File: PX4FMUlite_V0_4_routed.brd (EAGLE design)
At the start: 48.6 x 34.9 mm, 126 parts, among them J2 DF13-4P-1.25V, J201 DF13C-6P-1.25V, J202 DF13C-6P-1.25V, J203 DF13C-6P-1.25V, J3 DF13C-4P-1.25V, J302 DF13C-4P-1.25V, J401 DF13C-4P-1.25V, J403 DF13C-7P-1.25V, J405 DF13C-4P-1.25V, J802 DF13C-3P-1.25V, M3_MOUNT1101 MOUNT-HOLE3.1MM, M3_MOUNT1102 MOUNT-HOLE3.1MM, M3_MOUNT1103 MOUNT-HOLE3.1MM, M3_MOUNT1104 MOUNT-HOLE3.1MM, U101 STM32F4X7VX, U2 MAX3051, U401 MAX3051, X101 3.2x2.5 mm / 24 MHz / 15 ppm

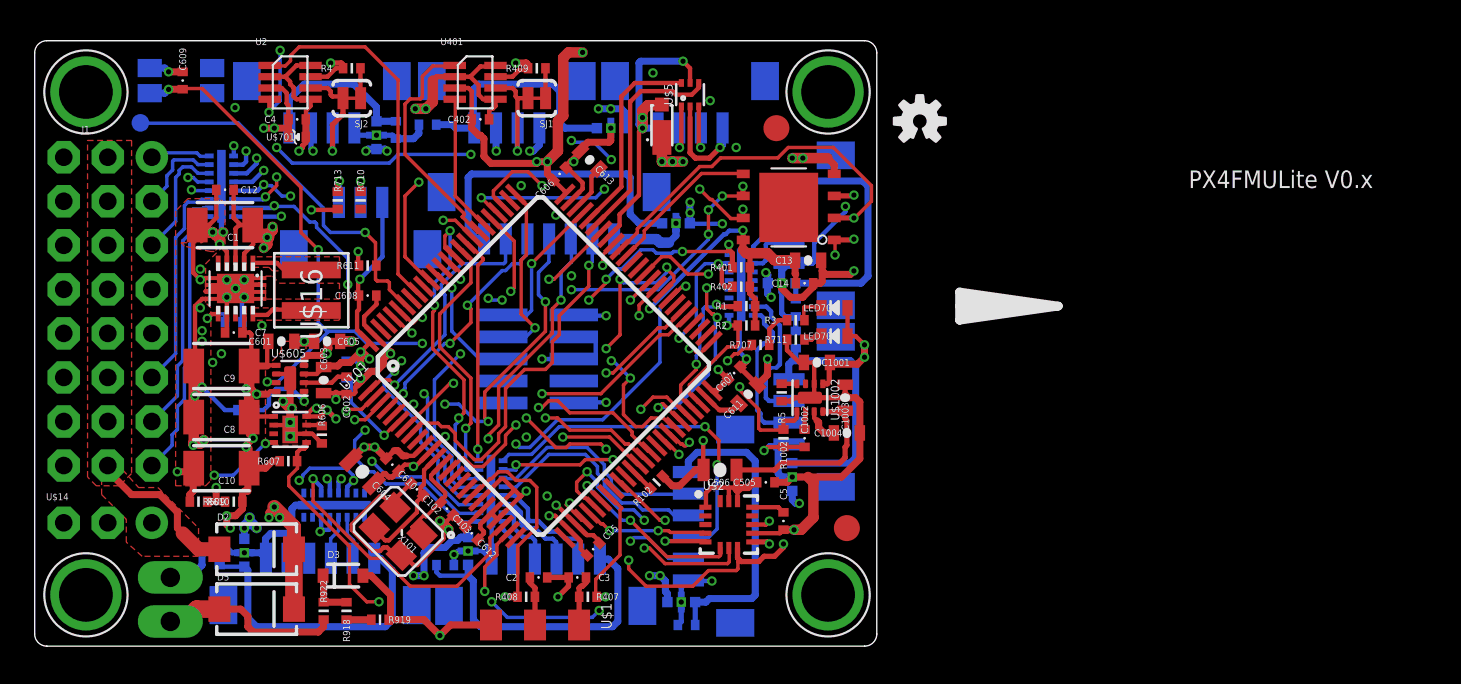
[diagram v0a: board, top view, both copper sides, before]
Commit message: Moved connector labeling
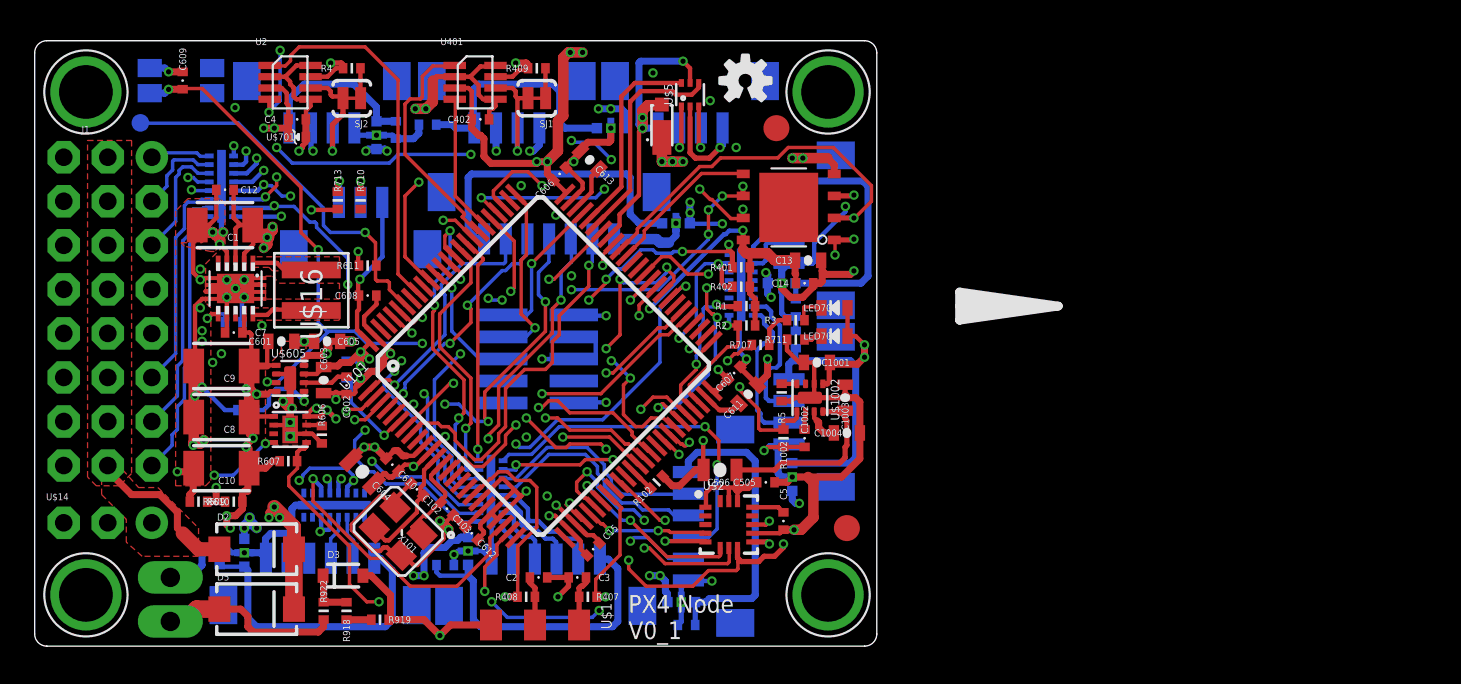
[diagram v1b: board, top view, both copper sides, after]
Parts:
- moved OSHW_LOGO 10.3 mm to (50.2, 35.4)
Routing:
- net FMU-VDD_3V3: vias 17 -> 18
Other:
- board text added: "PX4 Node V0_1"
- board text added: "SPKT/PPM"
- board text removed: "PX4FMULite V0.x"
- board text removed: "SPKT"
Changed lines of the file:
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@@
 <grid distance="4" unitdist="mil" unit="mm" style="dots" multiple="1" display="yes" altdistance="4" altunitdist="mil" altunit="mm"/>
 <layers>
-<layer number="1" name="Top" color="4" fill="1" visible="yes" active="yes"/>
+<layer number="1" name="Top" color="4" fill="1" visible="no" active="yes"/>
 <layer number="2" name="Ground" color="2" fill="10" visible="no" active="yes"/>
 <layer number="3" name="Horizontal" color="13" fill="15" visible="no" active="yes"/>
@@
 <layer number="19" name="Unrouted" color="14" fill="1" visible="no" active="yes"/>
 <layer number="20" name="Dimension" color="15" fill="1" visible="yes" active="yes"/>
-<layer number="21" name="tPlace" color="7" fill="1" visible="yes" active="yes"/>
+<layer number="21" name="tPlace" color="7" fill="1" visible="no" active="yes"/>
 <layer number="22" name="bPlace" color="7" fill="1" visible="yes" active="yes"/>
-<layer number="23" name="tOrigins" color="15" fill="1" visible="yes" active="yes"/>
+<layer number="23" name="tOrigins" color="15" fill="1" visible="no" active="yes"/>
 <layer number="24" name="bOrigins" color="15" fill="1" visible="yes" active="yes"/>
 <layer number="25" name="tNames" color="7" fill="1" visible="no" active="yes"/>
@@
 <layer number="37" name="tTest" color="7" fill="1" visible="no" active="yes"/>
 <layer number="38" name="bTest" color="7" fill="1" visible="no" active="yes"/>
-<layer number="39" name="tKeepout" color="4" fill="11" visible="yes" active="yes"/>
+<layer number="39" name="tKeepout" color="4" fill="11" visible="no" active="yes"/>
 <layer number="40" name="bKeepout" color="1" fill="11" visible="yes" active="yes"/>
-<layer number="41" name="tRestrict" color="4" fill="10" visible="yes" active="yes"/>
+<layer number="41" name="tRestrict" color="4" fill="10" visible="no" active="yes"/>
 <layer number="42" name="bRestrict" color="1" fill="10" visible="yes" active="yes"/>
 <layer number="43" name="vRestrict" color="2" fill="10" visible="no" active="yes"/>
@@
 <layer number="49" name="Reference" color="7" fill="1" visible="no" active="yes"/>
 <layer number="50" name="dxf" color="7" fill="1" visible="no" active="yes"/>
-<layer number="51" name="tDocu" color="7" fill="1" visible="yes" active="yes"/>
+<layer number="51" name="tDocu" color="7" fill="1" visible="no" active="yes"/>
 <layer number="52" name="bDocu" color="7" fill="1" visible="yes" active="yes"/>
 <layer number="53" name="tGND_GNDA" color="7" fill="9" visible="no" active="no"/>
@@
 <wire x1="62.992" y1="22.7584" x2="65.4304" y2="22.352" width="0.508" layer="21"/>
 <wire x1="64.2112" y1="22.352" x2="62.5856" y2="22.352" width="0.508" layer="21"/>
-<text x="75.7936" y="29.1592" size="1.016" layer="21" font="vector" ratio="15">PX4FMULite V0.x</text>
+<text x="43.4848" y="3.1496" size="1.016" layer="21" font="vector" ratio="15">PX4 Node
+V0_1</text>
 <text x="-1.9304" y="37.3888" size="0.762" layer="22" font="vector" ratio="15" rot="MR270">FMU B/E</text>
-<text x="68.1736" y="26.0096" size="0.762" layer="22" font="vector" ratio="15" rot="MR270">POWER</text>
-<text x="67.2592" y="15.9512" size="0.762" layer="22" font="vector" ratio="15" rot="MR270">SPI</text>
-<text x="48.1584" y="35.4584" size="0.762" layer="22" font="vector" ratio="15" rot="MR0">USB</text>
-<text x="67.8688" y="31.496" size="0.762" layer="22" font="vector" ratio="15" rot="MR270">SER1</text>
+<text x="14.732" y="8.5344" size="0.762" layer="22" font="vector" ratio="15" rot="MR180">POWER</text>
+<text x="46.228" y="28.6512" size="0.762" layer="22" font="vector" ratio="15" rot="MR90">SPI</text>
+<text x="51.5112" y="32.4104" size="0.762" layer="22" font="vector" ratio="15" rot="MR0">USB</text>
+<text x="61.468" y="18.1864" size="0.762" layer="22" font="vector" ratio="15" rot="MR270">SER1</text>
 <text x="-2.1336" y="25.4" size="0.762" layer="22" font="vector" ratio="15" rot="MR270">SER2</text>
-<text x="-2.032" y="30.3784" size="0.762" layer="22" font="vector" ratio="15" rot="MR270">SPKT</text>
+<text x="10.8712" y="11.7856" size="0.762" layer="22" font="vector" ratio="15" rot="MR180">SPKT/PPM</text>
 <text x="-2.2352" y="20.828" size="0.762" layer="22" font="vector" ratio="15" rot="MR270">SER4</text>
 <text x="37.3888" y="0.9144" size="0.762" layer="22" font="vector" ratio="15" rot="MR0">SER3</text>
-<text x="35.052" y="36.3728" size="0.762" layer="22" font="vector" ratio="15" rot="MR180">CAN1</text>
+<text x="31.0896" y="32.1056" size="0.762" layer="22" font="vector" ratio="15" rot="MR180">CAN1</text>
 <text x="61.5696" y="33.6296" size="0.762" layer="22" font="vector" ratio="15" rot="MR270">ADC</text>
-<text x="55.4736" y="27.8384" size="0.762" layer="22" font="vector" ratio="15" rot="MR270">I2C1</text>
+<text x="51.4096" y="29.464" size="0.762" layer="22" font="vector" ratio="15" rot="MR270">I2C1</text>
 <text x="61.2648" y="2.54" size="0.762" layer="22" font="vector" ratio="15" rot="MR270">AIR</text>
-<text x="29.3624" y="4.7752" size="0.762" layer="22" font="vector" ratio="15" rot="MR0">UART3 / GPS</text>
-<text x="49.6824" y="11.684" size="0.762" layer="22" font="vector" ratio="15" rot="MR270">UART1</text>
-<text x="36.9824" y="5.3848" size="0.762" layer="22" font="vector" ratio="15" rot="MR180">UART2</text>
-<text x="61.6712" y="29.5656" size="0.762" layer="22" font="vector" ratio="15" rot="MR270">AUX ADC</text>
+<text x="30.7848" y="8.8392" size="0.762" layer="22" font="vector" ratio="15" rot="MR0">UART3 / GPS</text>
+<text x="45.6184" y="14.224" size="0.762" layer="22" font="vector" ratio="15" rot="MR270">UART1</text>
+<text x="37.7952" y="9.8552" size="0.762" layer="22" font="vector" ratio="15" rot="MR180">UART2</text>
+<text x="29.7688" y="5.6896" size="0.762" layer="22" font="vector" ratio="15" rot="MR180">AUX ADC</text>
 <text x="27.0256" y="53.0352" size="0.762" layer="22" font="vector" ratio="15" rot="MR180">SAFETY</text>
-<text x="55.7784" y="17.0688" size="0.762" layer="22" font="vector" ratio="15" rot="MR270">I2C2</text>
-<text x="24.6888" y="35.9664" size="0.762" layer="22" font="vector" ratio="15" rot="MR180">CAN2</text>
+<text x="54.356" y="10.668" size="0.762" layer="22" font="vector" ratio="15" rot="MR180">I2C2</text>
+<text x="19.2024" y="33.2232" size="0.762" layer="22" font="vector" ratio="15" rot="MR180">CAN2</text>
 </plain>
 <attributes>
@@
 <attribute name="PARTNO" value="DF13C-6P-1.25V(20)" x="38.716" y="6.864" size="1.778" layer="28" rot="MR0" display="off"/>
 </element>
-<element name="OSHW_LOGO" library="pixhawk2" package="OSHW-LOGO-S" value="OSHW-LOGOS" x="60.2896" y="33.0152">
-<attribute name="PARTNO" value="*" x="60.2896" y="44.1912" size="1.778" layer="27" display="off"/>
-<attribute name="BOM" value="EXCLUDE" x="60.2896" y="44.1912" size="1.778" layer="27" display="off"/>
+<element name="OSHW_LOGO" library="pixhawk2" package="OSHW-LOGO-S" value="OSHW-LOGOS" x="50.2312" y="35.352">
+<attribute name="PARTNO" value="*" x="50.2312" y="46.528" size="1.778" layer="27" display="off"/>
+<attribute name="BOM" value="EXCLUDE" x="50.2312" y="46.528" size="1.778" layer="27" display="off"/>
 </element>
 <element name="M3_MOUNT1104" library="pixhawk2" package="MOUNT-HOLE3.1" value="MOUNT-HOLE3.1MM" x="12.2" y="5.7">
@@
 <attribute name="PARTNO" value="*" x="15.748" y="32.9184" size="1.778" layer="28" rot="MR0" display="off"/>
 <attribute name="BOM" value="EXCLUDE" x="15.748" y="32.9184" size="1.778" layer="28" rot="MR0" display="off"/>
-<attribute name="NAME" x="16.1424" y="33.1684" size="0.5" layer="22" font="vector" ratio="15" rot="MR180"/>
+<attribute name="NAME" x="15.9392" y="32.3556" size="0.5" layer="22" font="vector" ratio="15" rot="MR180"/>
 </element>
 <element name="J302" library="con-hirose-df13" package="DF13C-4P-1.25V" value="DF13C-4P-1.25V" x="47.0408" y="33.528" rot="MR180">
@@
 <wire x1="27.7448" y1="19.1944" x2="28.0416" y2="18.8976" width="0.254" layer="16"/>
 <wire x1="39.7256" y1="36.6776" x2="40.0304" y2="36.9824" width="0.6096" layer="1"/>
-<wire x1="40.0304" y1="36.9824" x2="40.8432" y2="36.9824" width="0.6096" layer="1"/>
+<wire x1="40.0304" y1="36.9824" x2="40.132" y2="36.9824" width="0.6096" layer="1"/>
 <via x="40.8432" y="36.9824" extent="1-16" drill="0.3"/>
-<wire x1="40.8432" y1="36.9824" x2="37.8968" y2="36.9824" width="0.6096" layer="15"/>
+<wire x1="40.132" y1="36.9824" x2="40.8432" y2="36.9824" width="0.6096" layer="1"/>
+<wire x1="40.8432" y1="36.9824" x2="40.132" y2="36.9824" width="0.6096" layer="15"/>
+<wire x1="40.132" y1="36.9824" x2="37.8968" y2="36.9824" width="0.6096" layer="15"/>
 <wire x1="37.8968" y1="36.9824" x2="37.7952" y2="37.084" width="0.4064" layer="15"/>
 <wire x1="37.7952" y1="37.084" x2="36.4744" y2="37.084" width="0.4064" layer="15"/>
@@
 <via x="42.2" y="21.8" extent="1-16" drill="0.3"/>
 <via x="44.7" y="22.2" extent="1-16" drill="0.3"/>
+<via x="40.132" y="36.9824" extent="1-16" drill="0.3"/>
 </signal>
 <signal name="OTG_FS_DP">
